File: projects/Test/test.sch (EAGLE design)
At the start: 49 parts, among them J1 284512-3, Y1 ECS-80-S-4X

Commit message: Final changes before ordering
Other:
- note added: "Use no resistors for 1x PWM"
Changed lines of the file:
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@@
 <text x="119.38" y="66.04" size="1.778" layer="91">SHB_1</text>
 <text x="195.58" y="63.5" size="1.778" layer="91">SHC_1</text>
+<text x="30.48" y="134.62" size="1.778" layer="91" rot="R90">Use no resistors for 1x PWM</text>
 </plain>
 <instances>

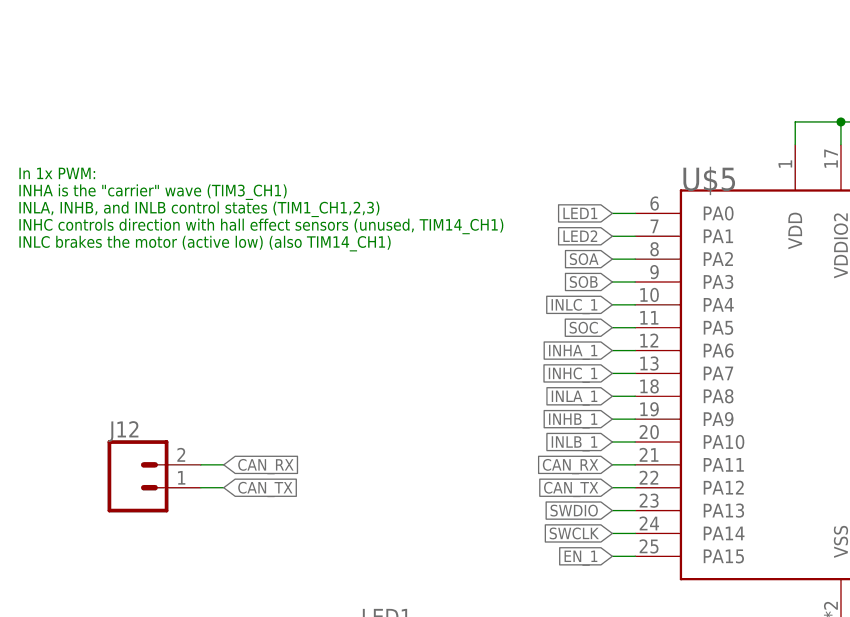
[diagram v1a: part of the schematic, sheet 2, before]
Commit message: Switch PWM lines to be optimized for 3x PWM
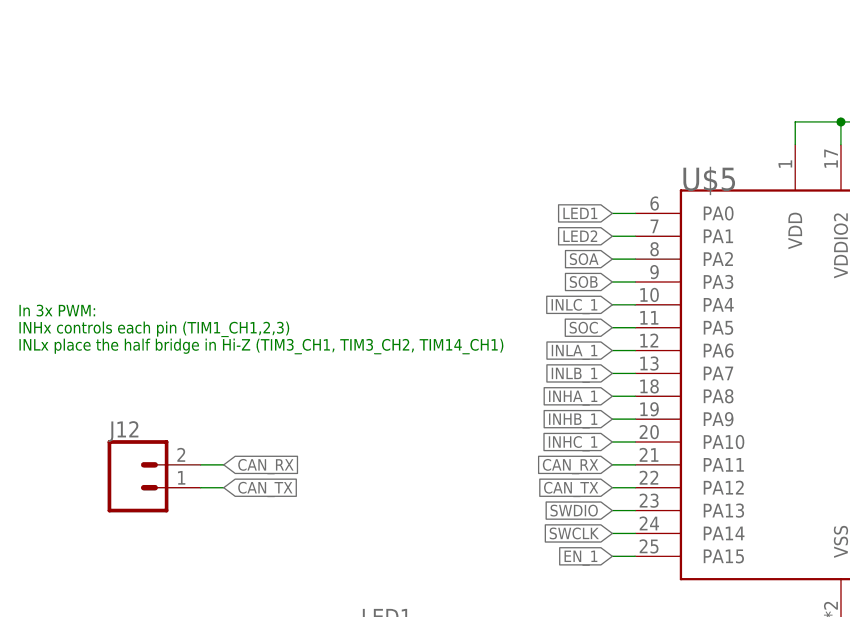
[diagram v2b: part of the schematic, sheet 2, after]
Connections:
- net INHA_1: now also U$5.PA8; no longer U$5.PA6
- net INHC_1: now also U$5.PA10; no longer U$5.PA7
- net INLA_1: now also U$5.PA6; no longer U$5.PA8
- net INLB_1: now also U$5.PA7; no longer U$5.PA10
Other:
- note added: "In 3x PWM: INHx controls each pin (TIM1_CH1,2,3) INLx place the half bridge in Hi-Z (TIM3_CH1, TIM3_CH2, TIM14_CH1)"
- note removed: "In 1x PWM: INHA is the "carrier" wave (TIM3_CH1) INLA, INHB, and INLB control states (TIM1_CH1,2,3) INHC controls direction with hall effect sensors (unused, TIM14_CH1) INLC brakes the motor (active low) (also TIM14_CH1)"
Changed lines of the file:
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@@
 <text x="111.76" y="154.94" size="1.778" layer="91">Pin 1 (VBAT)</text>
 <text x="132.08" y="154.94" size="1.778" layer="91">Pin 13 (VDDA)</text>
-<text x="25.4" y="101.6" size="1.27" layer="91" align="top-left">In 1x PWM:
-INHA is the "carrier" wave (TIM3_CH1)
-INLA, INHB, and INLB control states (TIM1_CH1,2,3)
-INHC controls direction with hall effect sensors (unused, TIM14_CH1)
-INLC brakes the motor (active low) (also TIM14_CH1)</text>
+<text x="25.4" y="86.36" size="1.27" layer="91" align="top-left">In 3x PWM:
+INHx controls each pin (TIM1_CH1,2,3)
+INLx place the half bridge in Hi-Z (TIM3_CH1, TIM3_CH2, TIM14_CH1)</text>
 </plain>
 <instances>
@@
 <net name="INHA_1" class="0">
 <segment>
+<wire x1="96.52" y1="30.48" x2="93.98" y2="30.48" width="0.1524" layer="91"/>
+<label x="93.98" y="30.48" size="1.27" layer="95" rot="R180" xref="yes"/>
+<pinref part="J2" gate="G$1" pin="1"/>
+</segment>
+<segment>
+<pinref part="U$5" gate="G$1" pin="PA8"/>
+<wire x1="93.98" y1="76.2" x2="91.44" y2="76.2" width="0.1524" layer="91"/>
+<label x="91.44" y="76.2" size="1.27" layer="95" rot="R180" xref="yes"/>
+</segment>
+</net>
+<net name="INHB_1" class="0">
+<segment>
+<wire x1="96.52" y1="20.32" x2="93.98" y2="20.32" width="0.1524" layer="91"/>
+<label x="93.98" y="20.32" size="1.27" layer="95" rot="R180" xref="yes"/>
+<pinref part="J3" gate="G$1" pin="1"/>
+</segment>
+<segment>
+<pinref part="U$5" gate="G$1" pin="PA9"/>
+<wire x1="93.98" y1="73.66" x2="91.44" y2="73.66" width="0.1524" layer="91"/>
+<label x="91.44" y="73.66" size="1.27" layer="95" rot="R180" xref="yes"/>
+</segment>
+</net>
+<net name="INLA_1" class="0">
+<segment>
+<wire x1="121.92" y1="30.48" x2="124.46" y2="30.48" width="0.1524" layer="91"/>
+<label x="124.46" y="30.48" size="1.27" layer="95" xref="yes"/>
+<pinref part="J5" gate="G$1" pin="1"/>
+</segment>
+<segment>
 <pinref part="U$5" gate="G$1" pin="PA6"/>
 <wire x1="93.98" y1="81.28" x2="91.44" y2="81.28" width="0.1524" layer="91"/>
 <label x="91.44" y="81.28" size="1.27" layer="95" rot="R180" xref="yes"/>
 </segment>
-<segment>
-<wire x1="96.52" y1="30.48" x2="93.98" y2="30.48" width="0.1524" layer="91"/>
-<label x="93.98" y="30.48" size="1.27" layer="95" rot="R180" xref="yes"/>
-<pinref part="J2" gate="G$1" pin="1"/>
-</segment>
-</net>
-<net name="INHB_1" class="0">
-<segment>
-<pinref part="U$5" gate="G$1" pin="PA9"/>
-<wire x1="93.98" y1="73.66" x2="91.44" y2="73.66" width="0.1524" layer="91"/>
-<label x="91.44" y="73.66" size="1.27" layer="95" rot="R180" xref="yes"/>
-</segment>
-<segment>
-<wire x1="96.52" y1="20.32" x2="93.98" y2="20.32" width="0.1524" layer="91"/>
-<label x="93.98" y="20.32" size="1.27" layer="95" rot="R180" xref="yes"/>
-<pinref part="J3" gate="G$1" pin="1"/>
-</segment>
-</net>
-<net name="INLA_1" class="0">
-<segment>
-<pinref part="U$5" gate="G$1" pin="PA8"/>
-<wire x1="93.98" y1="76.2" x2="91.44" y2="76.2" width="0.1524" layer="91"/>
-<label x="91.44" y="76.2" size="1.27" layer="95" rot="R180" xref="yes"/>
-</segment>
-<segment>
-<wire x1="121.92" y1="30.48" x2="124.46" y2="30.48" width="0.1524" layer="91"/>
-<label x="124.46" y="30.48" size="1.27" layer="95" xref="yes"/>
-<pinref part="J5" gate="G$1" pin="1"/>
-</segment>
 </net>
 <net name="INHC_1" class="0">
-<segment>
-<pinref part="U$5" gate="G$1" pin="PA7"/>
-<wire x1="93.98" y1="78.74" x2="91.44" y2="78.74" width="0.1524" layer="91"/>
-<label x="91.44" y="78.74" size="1.27" layer="95" rot="R180" xref="yes"/>
-</segment>
 <segment>
 <wire x1="96.52" y1="10.16" x2="93.98" y2="10.16" width="0.1524" layer="91"/>
 <label x="93.98" y="10.16" size="1.27" layer="95" rot="R180" xref="yes"/>
 <pinref part="J4" gate="G$1" pin="1"/>
+</segment>
+<segment>
+<pinref part="U$5" gate="G$1" pin="PA10"/>
+<wire x1="93.98" y1="71.12" x2="91.44" y2="71.12" width="0.1524" layer="91"/>
+<label x="91.44" y="71.12" size="1.27" layer="95" rot="R180" xref="yes"/>
 </segment>
 </net>
@@
 <net name="INLB_1" class="0">
 <segment>
-<pinref part="U$5" gate="G$1" pin="PA10"/>
-<wire x1="93.98" y1="71.12" x2="91.44" y2="71.12" width="0.1524" layer="91"/>
-<label x="91.44" y="71.12" size="1.27" layer="95" rot="R180" xref="yes"/>
-</segment>
-<segment>
 <wire x1="121.92" y1="20.32" x2="124.46" y2="20.32" width="0.1524" layer="91"/>
 <label x="124.46" y="20.32" size="1.27" layer="95" xref="yes"/>
 <pinref part="J6" gate="G$1" pin="1"/>
 </segment>
-</net>
+<segment>
+<pinref part="U$5" gate="G$1" pin="PA7"/>
+<wire x1="93.98" y1="78.74" x2="91.44" y2="78.74" width="0.1524" layer="91"/>
+<label x="91.44" y="78.74" size="1.27" layer="95" rot="R180" xref="yes"/>
+</segment>
+</net>
